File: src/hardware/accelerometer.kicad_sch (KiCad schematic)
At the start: 19 parts, among them U11 LIS2DUX12TR, U12 LIS2DUX12TR, U13 TPS22916BYFPR, U14 LIS2DUX12TR, U15 LIS2DUX12TR, Y3 DSC6003CE2A

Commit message: Changed footprints from 0603 to 0402
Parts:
- C32, C33, C34, C35, C36, C37, C38, C39, C40, C41, C42, C43, C44: footprint Capacitor_SMD:C_0603_1608Metric -> Capacitor_SMD:C_0504_1310Metric
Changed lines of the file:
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@@
 			)
 		)
-		(property "Footprint" "Capacitor_SMD:C_0603_1608Metric"
+		(property "Footprint" "Capacitor_SMD:C_0504_1310Metric"
 			(at 78.4352 77.47 0)
 			(effects
@@
 			)
 		)
-		(property "Footprint" "Capacitor_SMD:C_0603_1608Metric"
+		(property "Footprint" "Capacitor_SMD:C_0504_1310Metric"
 			(at 176.2252 147.32 0)
 			(effects
@@
 			)
 		)
-		(property "Footprint" "Capacitor_SMD:C_0603_1608Metric"
+		(property "Footprint" "Capacitor_SMD:C_0504_1310Metric"
 			(at 163.5252 77.47 0)
 			(effects
@@
 			)
 		)
-		(property "Footprint" "Capacitor_SMD:C_0603_1608Metric"
+		(property "Footprint" "Capacitor_SMD:C_0504_1310Metric"
 			(at 65.7352 137.16 0)
 			(effects
@@
 			)
 		)
-		(property "Footprint" "Capacitor_SMD:C_0603_1608Metric"
+		(property "Footprint" "Capacitor_SMD:C_0504_1310Metric"
 			(at 163.5252 137.16 0)
 			(effects
@@
 			)
 		)
-		(property "Footprint" "Capacitor_SMD:C_0603_1608Metric"
+		(property "Footprint" "Capacitor_SMD:C_0504_1310Metric"
 			(at 67.6148 170.18 0)
 			(effects
@@
 			)
 		)
-		(property "Footprint" "Capacitor_SMD:C_0603_1608Metric"
+		(property "Footprint" "Capacitor_SMD:C_0504_1310Metric"
 			(at 65.7352 77.47 0)
 			(effects
@@
 			)
 		)
-		(property "Footprint" "Capacitor_SMD:C_0603_1608Metric"
+		(property "Footprint" "Capacitor_SMD:C_0504_1310Metric"
 			(at 176.2252 137.16 0)
 			(effects
@@
 			)
 		)
-		(property "Footprint" "Capacitor_SMD:C_0603_1608Metric"
+		(property "Footprint" "Capacitor_SMD:C_0504_1310Metric"
 			(at 78.4352 137.16 0)
 			(effects
@@
 			)
 		)
-		(property "Footprint" "Capacitor_SMD:C_0603_1608Metric"
+		(property "Footprint" "Capacitor_SMD:C_0504_1310Metric"
 			(at 78.4352 147.32 0)
 			(effects
@@
 			)
 		)
-		(property "Footprint" "Capacitor_SMD:C_0603_1608Metric"
+		(property "Footprint" "Capacitor_SMD:C_0504_1310Metric"
 			(at 176.2252 87.63 0)
 			(effects
@@
 			)
 		)
-		(property "Footprint" "Capacitor_SMD:C_0603_1608Metric"
+		(property "Footprint" "Capacitor_SMD:C_0504_1310Metric"
 			(at 176.2252 77.47 0)
 			(effects
@@
 			)
 		)
-		(property "Footprint" "Capacitor_SMD:C_0603_1608Metric"
+		(property "Footprint" "Capacitor_SMD:C_0504_1310Metric"
 			(at 78.4352 87.63 0)
 			(effects

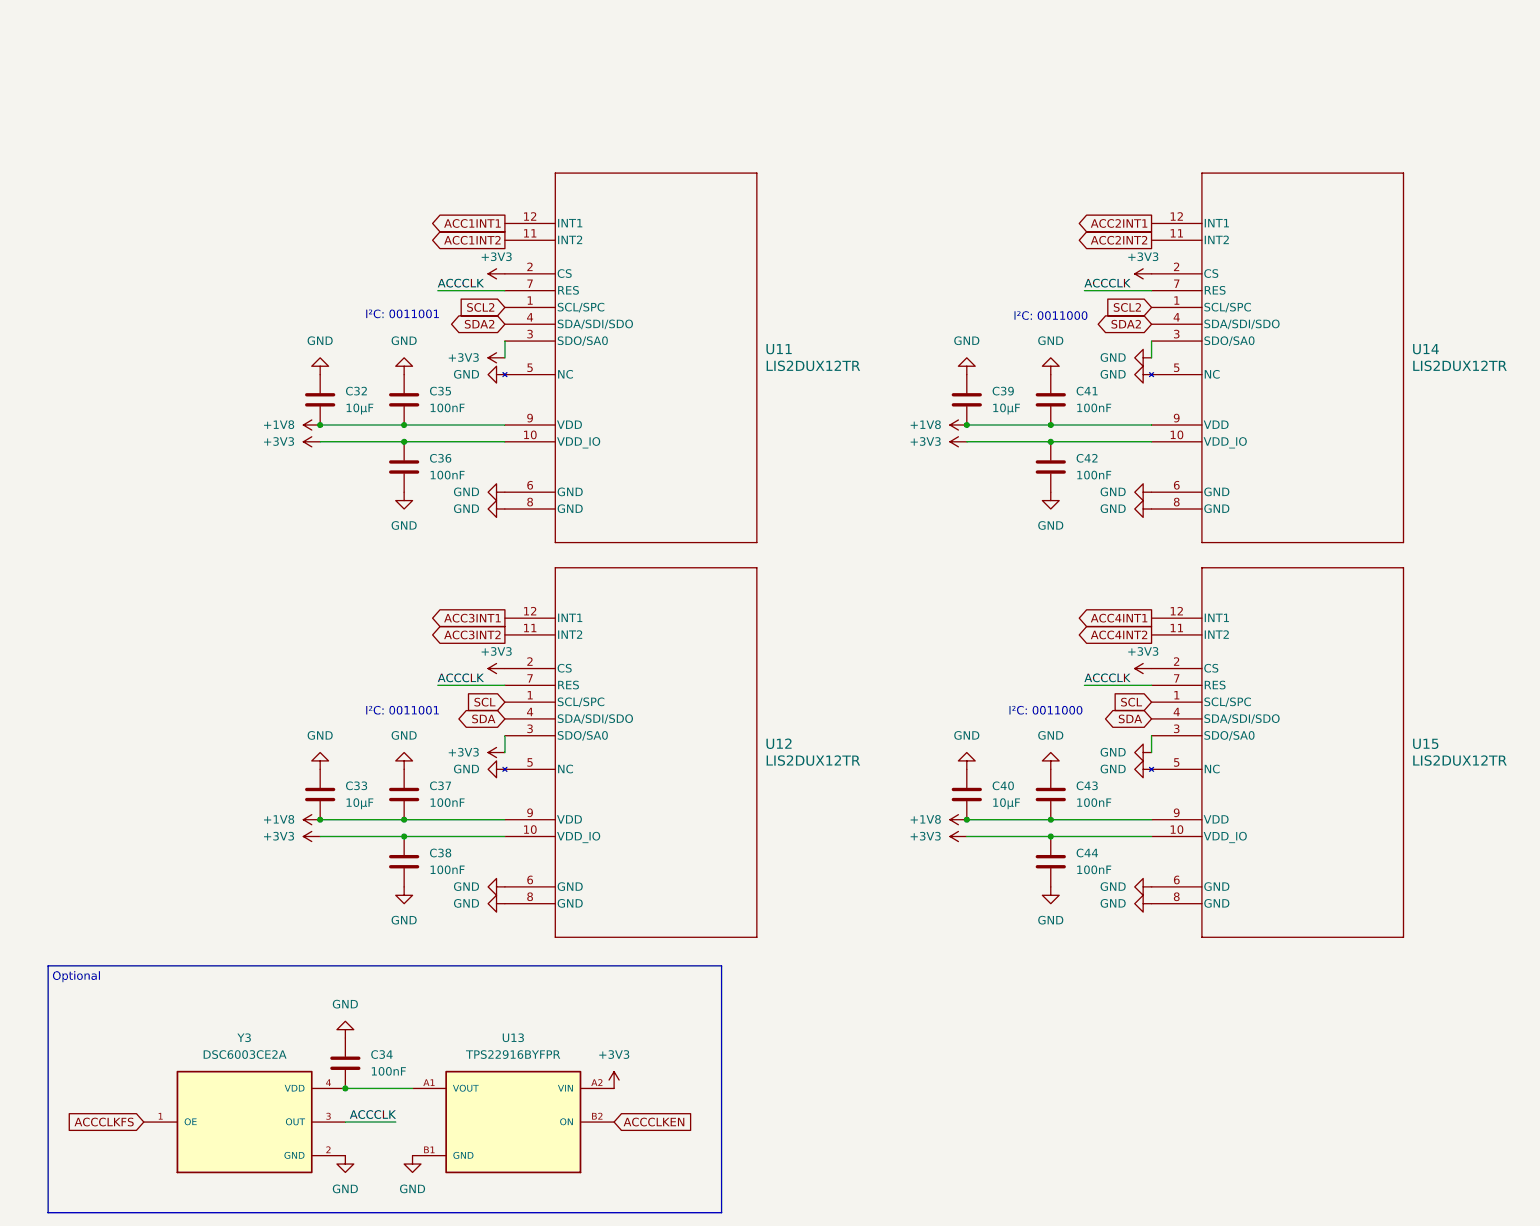
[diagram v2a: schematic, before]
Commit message: Replaced global labels with pin headers
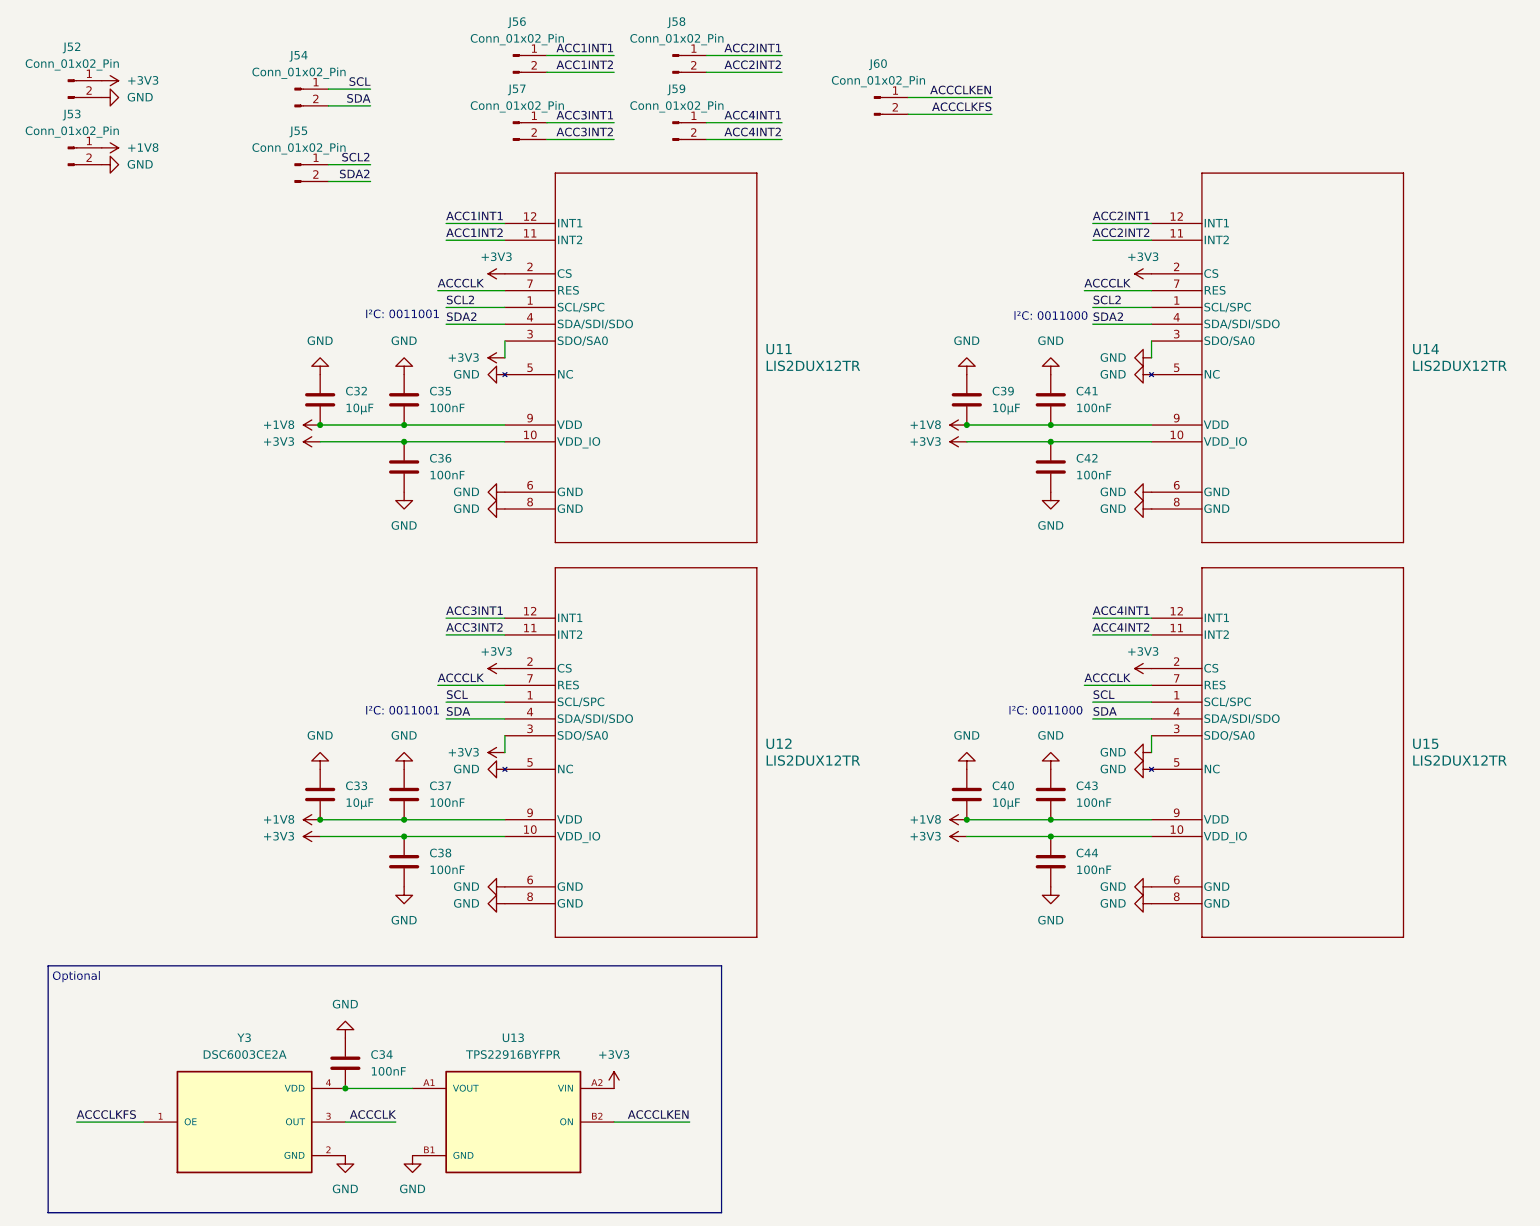
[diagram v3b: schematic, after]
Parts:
- added J52, J53, J54, J55, J56, J57, J58, J59, J60: Conn_01x02_Pin, symbol Connector:Conn_01x02_Pin
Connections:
- net +1V8: now also J53.1 (Pin_1)
- net +3V3: now also J52.1 (Pin_1)
- net ACC1INT1: now also J56.1 (Pin_1)
- net ACC1INT2: now also J56.2 (Pin_2)
- net ACC2INT1: now also J58.1 (Pin_1)
- net ACC2INT2: now also J58.2 (Pin_2)
- net ACC3INT1: now also J57.1 (Pin_1)
- net ACC3INT2: now also J57.2 (Pin_2)
- net ACC4INT1: now also J59.1 (Pin_1)
- net ACC4INT2: now also J59.2 (Pin_2)
- net ACCCLKEN: now also J60.1 (Pin_1)
- net ACCCLKFS: now also J60.2 (Pin_2)
- net GND: now also J52.2 (Pin_2), J53.2 (Pin_2)
- net SCL: now also J54.1 (Pin_1)
- net SCL2: now also J55.1 (Pin_1)
- net SDA: now also J54.2 (Pin_2)
- net SDA2: now also J55.2 (Pin_2)

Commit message: Reannotated schematic
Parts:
- renumbered C32 to C26, C33 to C27, C34 to C28, C35 to C29, C36 to C30, C37 to C31, C38 to C32, C39 to C33, C40 to C34, C41 to C35, C42 to C36, C43 to C37, C44 to C38, J52 to J39, J53 to J40, J54 to J41, J55 to J42, J56 to J43, J57 to J44, J58 to J45, J59 to J46, J60 to J47

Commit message: Assigned pin header footprints
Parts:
- J39, J40, J41, J42, J43, J44, J45, J46, J47: footprint (none) -> Connector_PinHeader_2.54mm:PinHeader_1x02_P2.54mm_Horizontal
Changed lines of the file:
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@@
 			)
 		)
-		(property "Footprint" ""
+		(property "Footprint" "Connector_PinHeader_2.54mm:PinHeader_1x02_P2.54mm_Horizontal"
 			(at 60.96 26.67 0)
 			(effects
@@
 			)
 		)
-		(property "Footprint" ""
+		(property "Footprint" "Connector_PinHeader_2.54mm:PinHeader_1x02_P2.54mm_Horizontal"
 			(at 118.11 21.59 0)
 			(effects
@@
 			)
 		)
-		(property "Footprint" ""
+		(property "Footprint" "Connector_PinHeader_2.54mm:PinHeader_1x02_P2.54mm_Horizontal"
 			(at 26.67 25.4 0)
 			(effects
@@
 			)
 		)
-		(property "Footprint" ""
+		(property "Footprint" "Connector_PinHeader_2.54mm:PinHeader_1x02_P2.54mm_Horizontal"
 			(at 148.59 27.94 0)
 			(effects
@@
 			)
 		)
-		(property "Footprint" ""
+		(property "Footprint" "Connector_PinHeader_2.54mm:PinHeader_1x02_P2.54mm_Horizontal"
 			(at 26.67 35.56 0)
 			(effects
@@
 			)
 		)
-		(property "Footprint" ""
+		(property "Footprint" "Connector_PinHeader_2.54mm:PinHeader_1x02_P2.54mm_Horizontal"
 			(at 60.96 38.1 0)
 			(effects
@@
 			)
 		)
-		(property "Footprint" ""
+		(property "Footprint" "Connector_PinHeader_2.54mm:PinHeader_1x02_P2.54mm_Horizontal"
 			(at 118.11 31.75 0)
 			(effects
@@
 			)
 		)
-		(property "Footprint" ""
+		(property "Footprint" "Connector_PinHeader_2.54mm:PinHeader_1x02_P2.54mm_Horizontal"
 			(at 93.98 31.75 0)
 			(effects
@@
 			)
 		)
-		(property "Footprint" ""
+		(property "Footprint" "Connector_PinHeader_2.54mm:PinHeader_1x02_P2.54mm_Horizontal"
 			(at 93.98 21.59 0)
 			(effects

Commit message: Reannotate
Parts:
- renumbered U11 to U10, U12 to U11, U13 to U12, U14 to U13, U15 to U14

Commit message: Changed pin headers to vertical
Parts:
- J39, J40, J41, J42, J43, J44, J45, J46, J47: footprint Connector_PinHeader_2.54mm:PinHeader_1x02_P2.54mm_Horizontal -> Connector_PinHeader_2.54mm:PinHeader_1x02_P2.54mm_Vertical
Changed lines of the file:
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@@
 			)
 		)
-		(property "Footprint" "Connector_PinHeader_2.54mm:PinHeader_1x02_P2.54mm_Horizontal"
+		(property "Footprint" "Connector_PinHeader_2.54mm:PinHeader_1x02_P2.54mm_Vertical"
 			(at 60.96 26.67 0)
 			(effects
@@
 			)
 		)
-		(property "Footprint" "Connector_PinHeader_2.54mm:PinHeader_1x02_P2.54mm_Horizontal"
+		(property "Footprint" "Connector_PinHeader_2.54mm:PinHeader_1x02_P2.54mm_Vertical"
 			(at 118.11 21.59 0)
 			(effects
@@
 			)
 		)
-		(property "Footprint" "Connector_PinHeader_2.54mm:PinHeader_1x02_P2.54mm_Horizontal"
+		(property "Footprint" "Connector_PinHeader_2.54mm:PinHeader_1x02_P2.54mm_Vertical"
 			(at 26.67 25.4 0)
 			(effects
@@
 			)
 		)
-		(property "Footprint" "Connector_PinHeader_2.54mm:PinHeader_1x02_P2.54mm_Horizontal"
+		(property "Footprint" "Connector_PinHeader_2.54mm:PinHeader_1x02_P2.54mm_Vertical"
 			(at 148.59 27.94 0)
 			(effects
@@
 			)
 		)
-		(property "Footprint" "Connector_PinHeader_2.54mm:PinHeader_1x02_P2.54mm_Horizontal"
+		(property "Footprint" "Connector_PinHeader_2.54mm:PinHeader_1x02_P2.54mm_Vertical"
 			(at 26.67 35.56 0)
 			(effects
@@
 			)
 		)
-		(property "Footprint" "Connector_PinHeader_2.54mm:PinHeader_1x02_P2.54mm_Horizontal"
+		(property "Footprint" "Connector_PinHeader_2.54mm:PinHeader_1x02_P2.54mm_Vertical"
 			(at 60.96 38.1 0)
 			(effects
@@
 			)
 		)
-		(property "Footprint" "Connector_PinHeader_2.54mm:PinHeader_1x02_P2.54mm_Horizontal"
+		(property "Footprint" "Connector_PinHeader_2.54mm:PinHeader_1x02_P2.54mm_Vertical"
 			(at 118.11 31.75 0)
 			(effects
@@
 			)
 		)
-		(property "Footprint" "Connector_PinHeader_2.54mm:PinHeader_1x02_P2.54mm_Horizontal"
+		(property "Footprint" "Connector_PinHeader_2.54mm:PinHeader_1x02_P2.54mm_Vertical"
 			(at 93.98 31.75 0)
 			(effects
@@
 			)
 		)
-		(property "Footprint" "Connector_PinHeader_2.54mm:PinHeader_1x02_P2.54mm_Horizontal"
+		(property "Footprint" "Connector_PinHeader_2.54mm:PinHeader_1x02_P2.54mm_Vertical"
 			(at 93.98 21.59 0)
 			(effects

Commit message: Fixed connector footprints; Changed conectors from 2.54 to 1.27
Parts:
- J37: renamed from J39; footprint Connector_PinHeader_2.54mm:PinHeader_1x02_P2.54mm_Vertical -> Connector_PinHeader_1.27mm:PinHeader_1x02_P1.27mm_Vertical
- J38: renamed from J40; footprint Connector_PinHeader_2.54mm:PinHeader_1x02_P2.54mm_Vertical -> Connector_PinHeader_1.27mm:PinHeader_1x02_P1.27mm_Vertical
- J39: renamed from J41; footprint Connector_PinHeader_2.54mm:PinHeader_1x02_P2.54mm_Vertical -> Connector_PinHeader_1.27mm:PinHeader_1x02_P1.27mm_Vertical
- J40: renamed from J42; footprint Connector_PinHeader_2.54mm:PinHeader_1x02_P2.54mm_Vertical -> Connector_PinHeader_1.27mm:PinHeader_1x02_P1.27mm_Vertical
- J41: renamed from J43; footprint Connector_PinHeader_2.54mm:PinHeader_1x02_P2.54mm_Vertical -> Connector_PinHeader_1.27mm:PinHeader_1x02_P1.27mm_Vertical
- J42: renamed from J44; footprint Connector_PinHeader_2.54mm:PinHeader_1x02_P2.54mm_Vertical -> Connector_PinHeader_1.27mm:PinHeader_1x02_P1.27mm_Vertical
- J43: renamed from J45; footprint Connector_PinHeader_2.54mm:PinHeader_1x02_P2.54mm_Vertical -> Connector_PinHeader_1.27mm:PinHeader_1x02_P1.27mm_Vertical
- J44: renamed from J46; footprint Connector_PinHeader_2.54mm:PinHeader_1x02_P2.54mm_Vertical -> Connector_PinHeader_1.27mm:PinHeader_1x02_P1.27mm_Vertical
- J45: renamed from J47; footprint Connector_PinHeader_2.54mm:PinHeader_1x02_P2.54mm_Vertical -> Connector_PinHeader_1.27mm:PinHeader_1x02_P1.27mm_Vertical
